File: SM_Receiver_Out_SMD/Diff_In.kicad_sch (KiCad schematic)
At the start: 14 parts, among them J7 RJ45, J8 RJ45, SW2 Terminators, U3 AM26C32IN

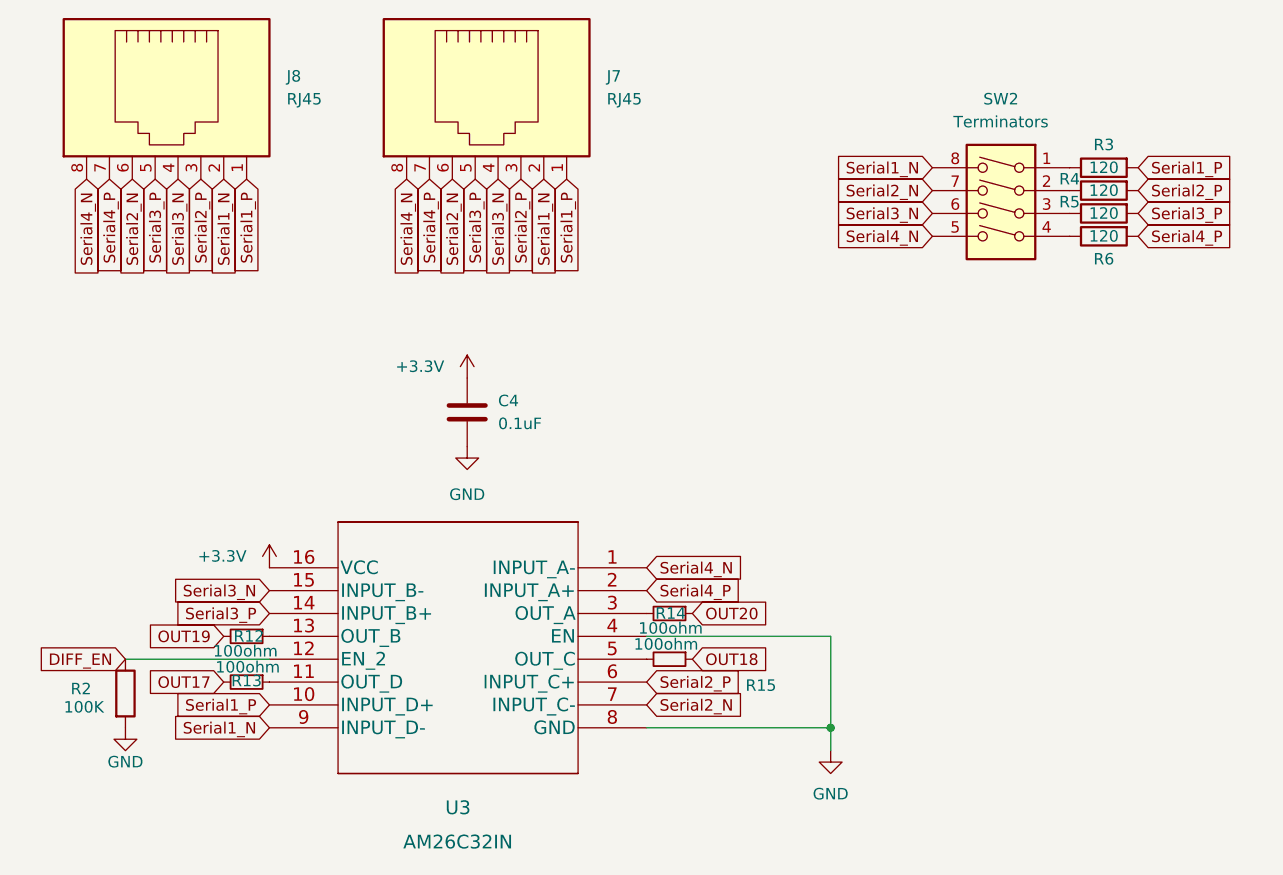
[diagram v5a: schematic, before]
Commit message: added 100 ohms
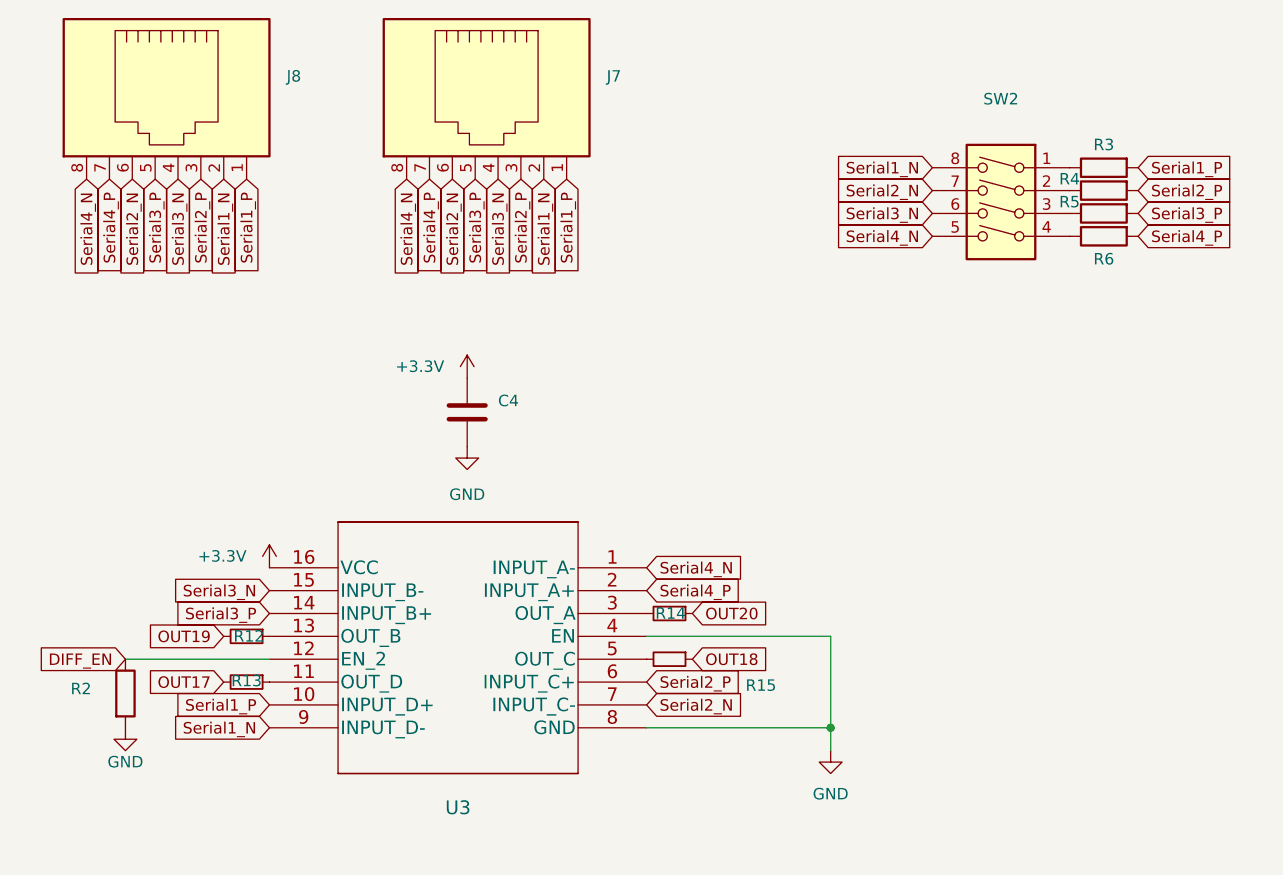
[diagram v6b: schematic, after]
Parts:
- C4: value 0.1uF -> (none); footprint Capacitor_SMD:C_0603_1608Metric_Pad1.08x0.95mm_HandSolder -> (none)
- J7, J8: value RJ45 -> (none); footprint Connector_RJ:RJ45_Amphenol_54602-x08_Horizontal -> (none)
- R12, R13, R14, R15: value 100ohm -> (none); footprint Resistor_SMD:R_0603_1608Metric_Pad0.98x0.95mm_HandSolder -> (none)
- R2: value 100K -> (none); footprint Resistor_SMD:R_0603_1608Metric_Pad0.98x0.95mm_HandSolder -> (none)
- R3, R4, R5, R6: value 120 -> (none); footprint Resistor_SMD:R_0603_1608Metric_Pad0.98x0.95mm_HandSolder -> (none)
- SW2: value Terminators -> (none); footprint Button_Switch_THT:SW_DIP_SPSTx04_Slide_6.7x11.72mm_W7.62mm_P2.54mm_LowProfile -> (none)
- U3: value AM26C32IN -> (none)
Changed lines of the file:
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@@
       (effects (font (size 1.524 1.524)))
     )
-    (property "Value" "AM26C32IN" (id 1) (at 142.875 137.16 0)
+    (property "Value" "" (id 1) (at 142.875 137.16 0)
       (effects (font (size 1.524 1.524)))
     )
@@
       (effects (font (size 1.27 1.27)) (justify right))
     )
-    (property "Value" "RJ45" (id 1) (at 159.385 54.6099 90)
+    (property "Value" "" (id 1) (at 159.385 54.6099 90)
       (effects (font (size 1.27 1.27)) (justify right))
     )
-    (property "Footprint" "Connector_RJ:RJ45_Amphenol_54602-x08_Horizontal" (id 2) (at 146.685 53.34 90)
+    (property "Footprint" "" (id 2) (at 146.685 53.34 90)
       (effects (font (size 1.27 1.27)) hide)
     )
@@
       (effects (font (size 1.27 1.27)) (justify left))
     )
-    (property "Value" "0.1uF" (id 1) (at 147.32 90.6779 0)
-      (effects (font (size 1.27 1.27)) (justify left))
-    )
-    (property "Footprint" "Capacitor_SMD:C_0603_1608Metric_Pad1.08x0.95mm_HandSolder" (id 2) (at 144.8562 93.218 0)
+    (property "Value" "" (id 1) (at 147.32 90.6779 0)
+      (effects (font (size 1.27 1.27)) (justify left))
+    )
+    (property "Footprint" "" (id 2) (at 144.8562 93.218 0)
       (effects (font (size 1.27 1.27)) hide)
     )
@@
     (in_bom yes) (on_board yes)
     (property "Reference" "R3" (id 0) (at 214.63 59.69 90))
-    (property "Value" "120" (id 1) (at 214.63 62.23 90))
-    (property "Footprint" "Resistor_SMD:R_0603_1608Metric_Pad0.98x0.95mm_HandSolder" (id 2) (at 214.63 60.452 90)
+    (property "Value" "" (id 1) (at 214.63 62.23 90))
+    (property "Footprint" "" (id 2) (at 214.63 60.452 90)
       (effects (font (size 1.27 1.27)) hide)
     )
@@
     (in_bom yes) (on_board yes)
     (property "Reference" "R4" (id 0) (at 210.82 63.5 90))
-    (property "Value" "120" (id 1) (at 214.63 64.77 90))
-    (property "Footprint" "Resistor_SMD:R_0603_1608Metric_Pad0.98x0.95mm_HandSolder" (id 2) (at 214.63 62.992 90)
+    (property "Value" "" (id 1) (at 214.63 64.77 90))
+    (property "Footprint" "" (id 2) (at 214.63 62.992 90)
       (effects (font (size 1.27 1.27)) hide)
     )
@@
     (in_bom yes) (on_board yes)
     (property "Reference" "R5" (id 0) (at 210.82 66.04 90))
-    (property "Value" "120" (id 1) (at 214.63 67.31 90))
-    (property "Footprint" "Resistor_SMD:R_0603_1608Metric_Pad0.98x0.95mm_HandSolder" (id 2) (at 214.63 65.532 90)
+    (property "Value" "" (id 1) (at 214.63 67.31 90))
+    (property "Footprint" "" (id 2) (at 214.63 65.532 90)
       (effects (font (size 1.27 1.27)) hide)
     )
@@
     (in_bom yes) (on_board yes)
     (property "Reference" "R6" (id 0) (at 214.63 72.39 90))
-    (property "Value" "120" (id 1) (at 214.63 69.85 90))
-    (property "Footprint" "Resistor_SMD:R_0603_1608Metric_Pad0.98x0.95mm_HandSolder" (id 2) (at 214.63 68.072 90)
+    (property "Value" "" (id 1) (at 214.63 69.85 90))
+    (property "Footprint" "" (id 2) (at 214.63 68.072 90)
       (effects (font (size 1.27 1.27)) hide)
     )
@@
       (effects (font (size 1.27 1.27)) (justify left))
     )
-    (property "Value" "100K" (id 1) (at 99.06 122.174 0)
-      (effects (font (size 1.27 1.27)) (justify left))
-    )
-    (property "Footprint" "Resistor_SMD:R_0603_1608Metric_Pad0.98x0.95mm_HandSolder" (id 2) (at 104.14 120.65 90)
+    (property "Value" "" (id 1) (at 99.06 122.174 0)
+      (effects (font (size 1.27 1.27)) (justify left))
+    )
+    (property "Footprint" "" (id 2) (at 104.14 120.65 90)
       (effects (font (size 1.27 1.27)) hide)
     )
@@
     (in_bom yes) (on_board yes)
     (property "Reference" "R15" (id 0) (at 176.53 119.761 90))
-    (property "Value" "100ohm" (id 1) (at 165.989 115.189 90))
-    (property "Footprint" "Resistor_SMD:R_0603_1608Metric_Pad0.98x0.95mm_HandSolder" (id 2) (at 166.37 116.84 0)
+    (property "Value" "" (id 1) (at 165.989 115.189 90))
+    (property "Footprint" "" (id 2) (at 166.37 116.84 0)
       (effects (font (size 1.27 1.27)) hide)
     )
@@
     (in_bom yes) (on_board yes) (fields_autoplaced)
     (property "Reference" "SW2" (id 0) (at 203.2 54.61 0))
-    (property "Value" "Terminators" (id 1) (at 203.2 57.15 0))
-    (property "Footprint" "Button_Switch_THT:SW_DIP_SPSTx04_Slide_6.7x11.72mm_W7.62mm_P2.54mm_LowProfile" (id 2) (at 203.2 67.31 0)
+    (property "Value" "" (id 1) (at 203.2 57.15 0))
+    (property "Footprint" "" (id 2) (at 203.2 67.31 0)
       (effects (font (size 1.27 1.27)) hide)
     )
@@
       (effects (font (size 1.27 1.27)) (justify right))
     )
-    (property "Value" "RJ45" (id 1) (at 123.825 54.6099 90)
+    (property "Value" "" (id 1) (at 123.825 54.6099 90)
       (effects (font (size 1.27 1.27)) (justify right))
     )
-    (property "Footprint" "Connector_RJ:RJ45_Amphenol_54602-x08_Horizontal" (id 2) (at 111.125 53.34 90)
+    (property "Footprint" "" (id 2) (at 111.125 53.34 90)
       (effects (font (size 1.27 1.27)) hide)
     )
@@
     (in_bom yes) (on_board yes)
     (property "Reference" "R13" (id 0) (at 119.38 119.253 90))
-    (property "Value" "100ohm" (id 1) (at 119.507 117.729 90))
-    (property "Footprint" "Resistor_SMD:R_0603_1608Metric_Pad0.98x0.95mm_HandSolder" (id 2) (at 119.38 119.38 0)
+    (property "Value" "" (id 1) (at 119.507 117.729 90))
+    (property "Footprint" "" (id 2) (at 119.38 119.38 0)
       (effects (font (size 1.27 1.27)) hide)
     )
@@
     (in_bom yes) (on_board yes)
     (property "Reference" "R12" (id 0) (at 119.634 114.3 90))
-    (property "Value" "100ohm" (id 1) (at 119.253 115.951 90))
-    (property "Footprint" "Resistor_SMD:R_0603_1608Metric_Pad0.98x0.95mm_HandSolder" (id 2) (at 119.38 114.3 0)
+    (property "Value" "" (id 1) (at 119.253 115.951 90))
+    (property "Footprint" "" (id 2) (at 119.38 114.3 0)
       (effects (font (size 1.27 1.27)) hide)
     )
@@
     (in_bom yes) (on_board yes)
     (property "Reference" "R14" (id 0) (at 166.497 111.76 90))
-    (property "Value" "100ohm" (id 1) (at 166.497 113.411 90))
-    (property "Footprint" "Resistor_SMD:R_0603_1608Metric_Pad0.98x0.95mm_HandSolder" (id 2) (at 166.37 111.76 0)
-      (effects (font (size 1.27 1.27)) hide)
-    )
+    (property "Value" "" (id 1) (at 166.497 113.411 90))
+    (property "Footprint" "" (id 2) (at 166.37 111.76 0)
+      (effects (font (size 1.27 1.27)) hide)
+    )

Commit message: fix RJ45 PN
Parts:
- J7, J8: LCSC_PN C305972 -> C2938579
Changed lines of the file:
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@@
       (effects (font (size 1.27 1.27)) hide)
     )
-    (property "LCSC_PN" "C305972" (id 6) (at 147.32 53.34 0)
+    (property "LCSC_PN" "C2938579" (id 6) (at 147.32 53.34 0)
       (effects (font (size 1.27 1.27)) hide)
     )
@@
       (effects (font (size 1.27 1.27)) hide)
     )
-    (property "LCSC_PN" "C305972" (id 6) (at 111.76 53.34 0)
-      (effects (font (size 1.27 1.27)) hide)
-    )
+    (property "LCSC_PN" "C2938579" (id 6) (at 111.76 53.34 0)
+      (effects (font (size 1.27 1.27)) hide)
+    )
